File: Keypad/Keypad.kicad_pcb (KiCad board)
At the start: 2 copper layers, 50 x 35 mm, 3 parts, among them J1 locked

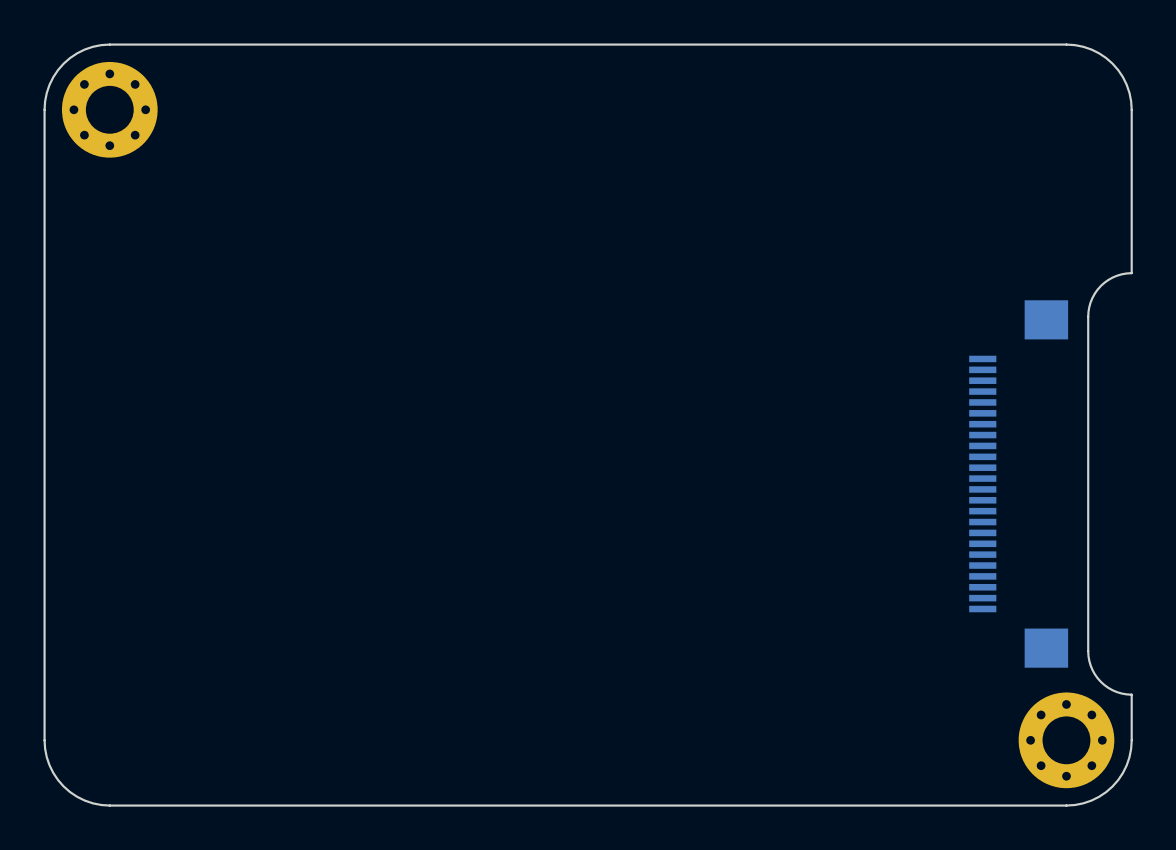
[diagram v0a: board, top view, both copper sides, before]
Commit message: Roughly places components in the keypad PCB
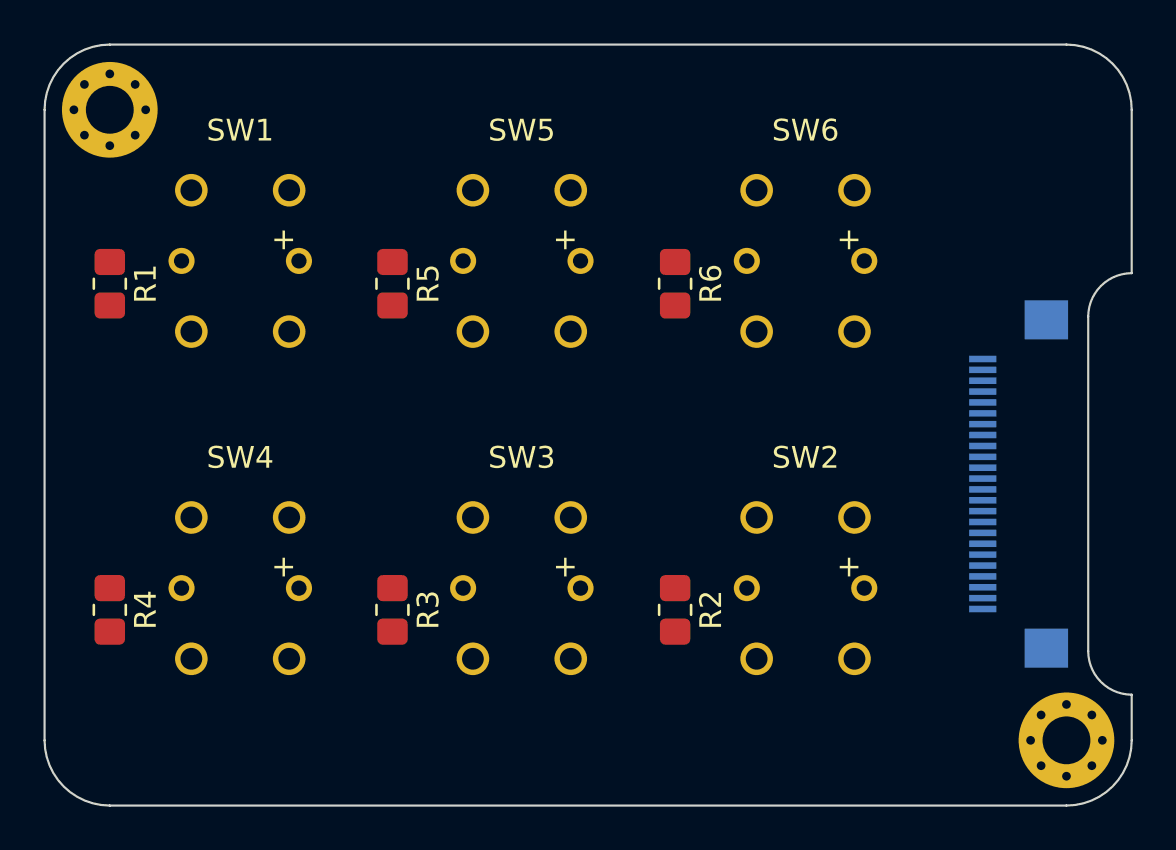
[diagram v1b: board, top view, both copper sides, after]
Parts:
- added R1: 100Ω, Resistor_SMD:R_0805_2012Metric_Pad1.20x1.40mm_HandSolder, F.Cu at (123.0, 91.0)
- added R2: 100Ω, Resistor_SMD:R_0805_2012Metric_Pad1.20x1.40mm_HandSolder, F.Cu at (149.0, 106.0)
- added R3: 100Ω, Resistor_SMD:R_0805_2012Metric_Pad1.20x1.40mm_HandSolder, F.Cu at (136.0, 106.0)
- added R4: 100Ω, Resistor_SMD:R_0805_2012Metric_Pad1.20x1.40mm_HandSolder, F.Cu at (123.0, 106.0)
- added R5: 100Ω, Resistor_SMD:R_0805_2012Metric_Pad1.20x1.40mm_HandSolder, F.Cu at (136.0, 91.0)
- added R6: 100Ω, Resistor_SMD:R_0805_2012Metric_Pad1.20x1.40mm_HandSolder, F.Cu at (149.0, 91.0)
- added SW1: TL1240GQ1JCLR, GameOver:TL1240GQ1JCLR, F.Cu at (129.0, 90.0)
- added SW2: TL1240GQ1JCLR, GameOver:TL1240GQ1JCLR, F.Cu at (155.0, 105.0)
- added SW3: TL1240GQ1JCLR, GameOver:TL1240GQ1JCLR, F.Cu at (141.9, 105.0)
- added SW4: TL1240GQ1JCLR, GameOver:TL1240GQ1JCLR, F.Cu at (129.0, 105.0)
- added SW5: TL1240GQ1JCLR, GameOver:TL1240GQ1JCLR, F.Cu at (141.9, 90.0)
- added SW6: TL1240GQ1JCLR, GameOver:TL1240GQ1JCLR, F.Cu at (155.0, 90.0)
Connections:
- J1 pad 17: unconnected-(J1-IO33) -> SW_6
- J1 pad 18: unconnected-(J1-IO25) -> LED_6
- J1 pad 19: unconnected-(J1-IO26) -> SW_4
- J1 pad 20: unconnected-(J1-IO27) -> LED_4
- J1 pad 21: unconnected-(J1-IO2) -> SW_2
- J1 pad 22: unconnected-(J1-IO15) -> LED_2
- J1 pad 3: unconnected-(J1-IO23) -> SW_1
- J1 pad 4: unconnected-(J1-IO22) -> LED_1
- J1 pad 5: unconnected-(J1-IO21) -> SW_3
- J1 pad 6: unconnected-(J1-IO19) -> LED_3
- J1 pad 7: unconnected-(J1-IO5) -> SW_5
- J1 pad 8: unconnected-(J1-IO18) -> LED_5

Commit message: Reorganizes components for better placement in keypad
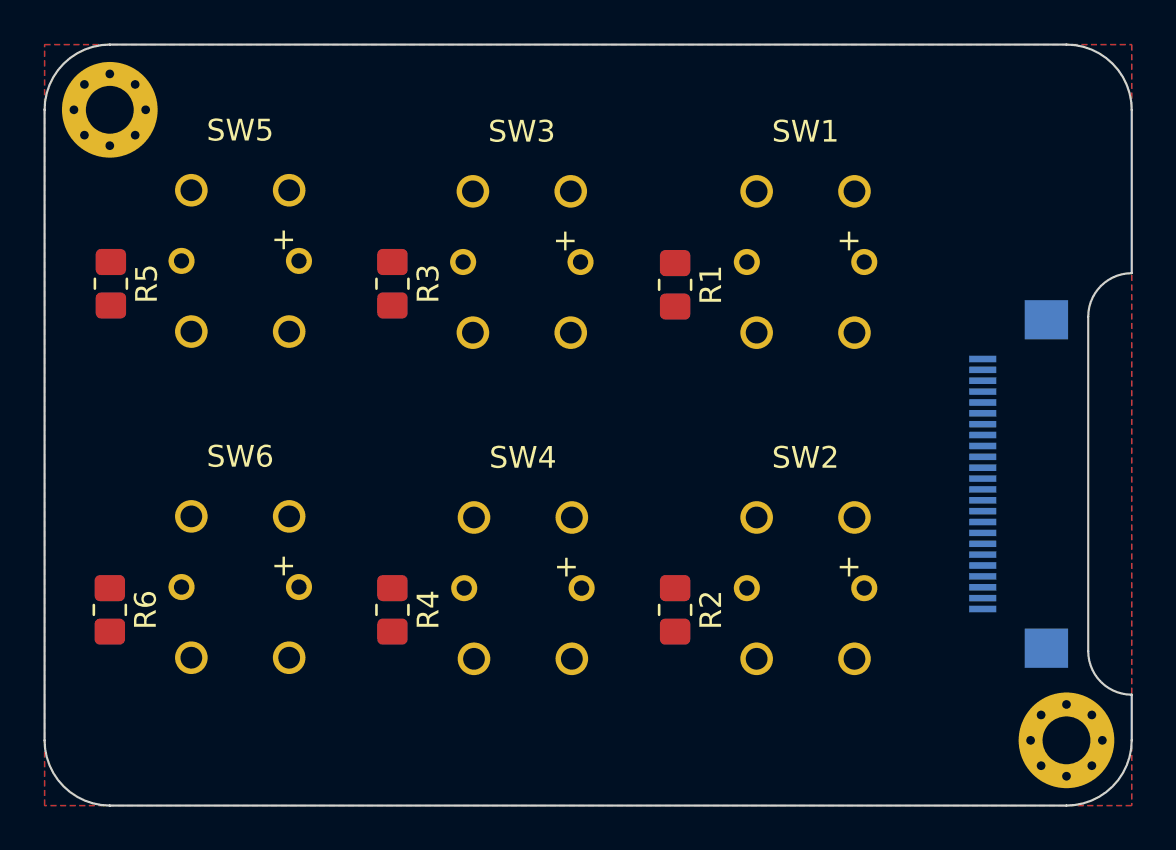
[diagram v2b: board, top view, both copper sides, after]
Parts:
- moved R6 30.0 mm to (123.0, 106.0)
- moved SW6 30.0 mm to (129.0, 105.0)
- moved R1 26.0 mm to (149.0, 91.0)
- moved SW1 26.0 mm to (155.0, 90.0)
- moved R3 15.0 mm to (136.0, 91.0)
- moved SW3 15.0 mm to (141.9, 90.0)
- moved R4 13.0 mm to (136.0, 106.0)
- moved SW4 13.0 mm to (142.0, 105.0)
- moved R5 13.0 mm to (123.0, 91.0)
- moved SW5 12.9 mm to (129.0, 90.0)
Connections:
- SW1 pad 3: SW_1 -> unconnected-(SW1-Pad3)
- SW2 pad 4: SW_2 -> unconnected-(SW2-Pad4)
- SW3 pad 3: SW_3 -> unconnected-(SW3-Pad3)
- SW4 pad 4: SW_4 -> unconnected-(SW4-Pad4)
- SW5 pad 3: SW_5 -> unconnected-(SW5-Pad3)
- SW6 pad 4: SW_6 -> unconnected-(SW6-Pad4)
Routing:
- added copper zone on B.Cu, net +3V3
- added copper zone on F.Cu, net GND
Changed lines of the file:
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@@
   (net 25 "Net-(SW5--)")
   (net 26 "Net-(SW6--)")
+  (net 27 "unconnected-(SW1-Pad3)")
+  (net 28 "unconnected-(SW2-Pad4)")
+  (net 29 "unconnected-(SW3-Pad3)")
+  (net 30 "unconnected-(SW4-Pad4)")
+  (net 31 "unconnected-(SW5-Pad3)")
+  (net 32 "unconnected-(SW6-Pad4)")
   (footprint "Resistor_SMD:R_0805_2012Metric_Pad1.20x1.40mm_HandSolder" (layer "F.Cu")
-    (at 136 91 -90)
+    (at 123.05 91 -90)
     (descr "Resistor SMD 0805 (2012 Metric), square (rectangular) end terminal, IPC_7351 nominal with elongated pad for handsoldering. (Body size source: IPC-SM-782 page 72, https://www.pcb-3d.com/wordpress/wp-content/uploads/ipc-sm-782a_amendment_1_and_2.pdf), generated with kicad-footprint-generator")
     (tags "resistor handsolder")
@@
       (net 19 "SW_2") (pinfunction "3") (pintype "passive"))
     (pad "4" thru_hole circle (at -2.25 3.25) (size 1.5 1.5) (drill 1) (layers *.Cu *.Mask)
-      (net 19 "SW_2") (pinfunction "4") (pintype "passive"))
+      (net 28 "unconnected-(SW2-Pad4)") (pinfunction "4") (pintype "passive+no_connect"))
     (pad "5" thru_hole circle (at 2.7 0) (size 1.2 1.2) (drill 0.7) (layers *.Cu *.Mask)
       (net 20 "LED_2") (pinfunction "+") (pintype "passive"))
@@
   )
   (footprint "GameOver:TL1240GQ1JCLR" (layer "F.Cu")
-    (at 141.95 105)
+    (at 141.95 90)
     (property "Sheetfile" "Keypad.kicad_sch")
     (property "Sheetname" "")
@@
       (net 2 "+3V3") (pinfunction "2") (pintype "passive"))
     (pad "3" thru_hole circle (at -2.25 -3.25) (size 1.5 1.5) (drill 1) (layers *.Cu *.Mask)
-      (net 5 "SW_3") (pinfunction "3") (pintype "passive"))
+      (net 29 "unconnected-(SW3-Pad3)") (pinfunction "3") (pintype "passive+no_connect"))
     (pad "4" thru_hole circle (at -2.25 3.25) (size 1.5 1.5) (drill 1) (layers *.Cu *.Mask)
       (net 5 "SW_3") (pinfunction "4") (pintype "passive"))
@@
   )
   (footprint "Resistor_SMD:R_0805_2012Metric_Pad1.20x1.40mm_HandSolder" (layer "F.Cu")
-    (at 123 106 -90)
+    (at 136 106 -90)
     (descr "Resistor SMD 0805 (2012 Metric), square (rectangular) end terminal, IPC_7351 nominal with elongated pad for handsoldering. (Body size source: IPC-SM-782 page 72, https://www.pcb-3d.com/wordpress/wp-content/uploads/ipc-sm-782a_amendment_1_and_2.pdf), generated with kicad-footprint-generator")
     (tags "resistor handsolder")
@@
   )
   (footprint "GameOver:TL1240GQ1JCLR" (layer "F.Cu")
-    (at 129 105)
+    (at 142 105)
     (property "Sheetfile" "Keypad.kicad_sch")
     (property "Sheetname" "")
@@
       (net 14 "SW_4") (pinfunction "3") (pintype "passive"))
     (pad "4" thru_hole circle (at -2.25 3.25) (size 1.5 1.5) (drill 1) (layers *.Cu *.Mask)
-      (net 14 "SW_4") (pinfunction "4") (pintype "passive"))
+      (net 30 "unconnected-(SW4-Pad4)") (pinfunction "4") (pintype "passive+no_connect"))
     (pad "5" thru_hole circle (at 2.7 0) (size 1.2 1.2) (drill 0.7) (layers *.Cu *.Mask)
       (net 18 "LED_4") (pinfunction "+") (pintype "passive"))
@@
   )
   (footprint "Resistor_SMD:R_0805_2012Metric_Pad1.20x1.40mm_HandSolder" (layer "F.Cu")
-    (at 136 106 -90)
+    (at 136 91 -90)
     (descr "Resistor SMD 0805 (2012 Metric), square (rectangular) end terminal, IPC_7351 nominal with elongated pad for handsoldering. (Body size source: IPC-SM-782 page 72, https://www.pcb-3d.com/wordpress/wp-content/uploads/ipc-sm-782a_amendment_1_and_2.pdf), generated with kicad-footprint-generator")
     (tags "resistor handsolder")
@@
   )
   (footprint "Resistor_SMD:R_0805_2012Metric_Pad1.20x1.40mm_HandSolder" (layer "F.Cu")
-    (at 123 91 -90)
+    (at 149 91.05 -90)
     (descr "Resistor SMD 0805 (2012 Metric), square (rectangular) end terminal, IPC_7351 nominal with elongated pad for handsoldering. (Body size source: IPC-SM-782 page 72, https://www.pcb-3d.com/wordpress/wp-content/uploads/ipc-sm-782a_amendment_1_and_2.pdf), generated with kicad-footprint-generator")
     (tags "resistor handsolder")
@@
   )
   (footprint "Resistor_SMD:R_0805_2012Metric_Pad1.20x1.40mm_HandSolder" (layer "F.Cu")
-    (at 149 91 -90)
+    (at 123 106 -90)
     (descr "Resistor SMD 0805 (2012 Metric), square (rectangular) end terminal, IPC_7351 nominal with elongated pad for handsoldering. (Body size source: IPC-SM-782 page 72, https://www.pcb-3d.com/wordpress/wp-content/uploads/ipc-sm-782a_amendment_1_and_2.pdf), generated with kicad-footprint-generator")
     (tags "resistor handsolder")
@@
   )
   (footprint "GameOver:TL1240GQ1JCLR" (layer "F.Cu")
-    (at 155 89.95)
+    (at 129 104.95)
     (property "Sheetfile" "Keypad.kicad_sch")
     (property "Sheetname" "")
@@
         (effects (font (size 1 1) (thickness 0.15)))
     )
-    (fp_text value "TL1240GQ1JCLR" (at 0 12 unlocked) (layer "F.Fab")
+    (fp_text value "TL1240GQ1JCLR" (at 0 6.05 unlocked) (layer "F.Fab")
         (effects (font (size 1 1) (thickness 0.15)))
     )
@@
         (effects (font (size 1 1) (thickness 0.15)))
     )
-    (fp_text user "${REFERENCE}" (at 0 14 unlocked) (layer "F.Fab")
+    (fp_text user "${REFERENCE}" (at 0 8.05 unlocked) (layer "F.Fab")
         (effects (font (size 1 1) (thickness 0.15)))
     )
@@
       (net 9 "SW_6") (pinfunction "3") (pintype "passive"))
     (pad "4" thru_hole circle (at -2.25 3.25) (size 1.5 1.5) (drill 1) (layers *.Cu *.Mask)
-      (net 9 "SW_6") (pinfunction "4") (pintype "passive"))
+      (net 32 "unconnected-(SW6-Pad4)") (pinfunction "4") (pintype "passive+no_connect"))
     (pad "5" thru_hole circle (at 2.7 0) (size 1.2 1.2) (drill 0.7) (layers *.Cu *.Mask)
       (net 13 "LED_6") (pinfunction "+") (pintype "passive"))
@@
   )
   (footprint "GameOver:TL1240GQ1JCLR" (layer "F.Cu")
-    (at 129 89.95)
+    (at 155 90)
     (property "Sheetfile" "Keypad.kicad_sch")
     (property "Sheetname" "")
@@
         (effects (font (size 1 1) (thickness 0.15)))
     )
-    (fp_text value "TL1240GQ1JCLR" (at 0 12 unlocked) (layer "F.Fab")
+    (fp_text value "TL1240GQ1JCLR" (at 0 6 unlocked) (layer "F.Fab")
         (effects (font (size 1 1) (thickness 0.15)))
     )
@@
         (effects (font (size 1 1) (thickness 0.15)))
     )
-    (fp_text user "${REFERENCE}" (at 0 14 unlocked) (layer "F.Fab")
+    (fp_text user "${REFERENCE}" (at 0 8 unlocked) (layer "F.Fab")
         (effects (font (size 1 1) (thickness 0.15)))
     )
@@
       (net 2 "+3V3") (pinfunction "2") (pintype "passive"))
     (pad "3" thru_hole circle (at -2.25 -3.25) (size 1.5 1.5) (drill 1) (layers *.Cu *.Mask)
-      (net 3 "SW_1") (pinfunction "3") (pintype "passive"))
+      (net 27 "unconnected-(SW1-Pad3)") (pinfunction "3") (pintype "passive+no_connect"))
     (pad "4" thru_hole circle (at -2.25 3.25) (size 1.5 1.5) (drill 1) (layers *.Cu *.Mask)
       (net 3 "SW_1") (pinfunction "4") (pintype "passive"))
@@
   )
   (footprint "GameOver:TL1240GQ1JCLR" (layer "F.Cu")
-    (at 141.95 89.95)
+    (at 129 89.95)
     (property "Sheetfile" "Keypad.kicad_sch")
     (property "Sheetname" "")
@@
         (effects (font (size 1 1) (thickness 0.15)))
     )
-    (fp_text value "TL1240GQ1JCLR" (at 0 12 unlocked) (layer "F.Fab")
+    (fp_text value "TL1240GQ1JCLR" (at 0 6.05 unlocked) (layer "F.Fab")
         (effects (font (size 1 1) (thickness 0.15)))
     )
@@
         (effects (font (size 1 1) (thickness 0.15)))
     )
-    (fp_text user "${REFERENCE}" (at 0 14 unlocked) (layer "F.Fab")
+    (fp_text user "${REFERENCE}" (at 0 8.05 unlocked) (layer "F.Fab")
         (effects (font (size 1 1) (thickness 0.15)))
     )
@@
       (net 2 "+3V3") (pinfunction "2") (pintype "passive"))
     (pad "3" thru_hole circle (at -2.25 -3.25) (size 1.5 1.5) (drill 1) (layers *.Cu *.Mask)
-      (net 7 "SW_5") (pinfunction "3") (pintype "passive"))
+      (net 31 "unconnected-(SW5-Pad3)") (pinfunction "3") (pintype "passive+no_connect"))
     (pad "4" thru_hole circle (at -2.25 3.25) (size 1.5 1.5) (drill 1) (layers *.Cu *.Mask)
       (net 7 "SW_5") (pinfunction "4") (pintype "passive"))
@@
   (gr_arc locked (start 167 80) (mid 169.12132 80.87868) (end 170 83)
     (stroke (width 0.1) (type default)) (layer "Edge.Cuts"))
+  (zone (net 1) (net_name "GND") (layer "F.Cu") (hatch edge 0.508)
+    (connect_pads (clearance 0.508))
+    (min_thickness 0.254) (filled_areas_thickness no)
+    (fill yes (thermal_gap 0.508) (thermal_bridge_width 0.508) (island_removal_mode 2) (island_area_min 10))
+    (polygon
+      (pts
+        (xy 170 115)
+        (xy 120 115)
+        (xy 120 80)
+        (xy 170 80)
+      )
+    )
+  )
+  (zone (net 2) (net_name "+3V3") (layer "B.Cu") (hatch edge 0.508)
+    (connect_pads (clearance 0.508))
+    (min_thickness 0.254) (filled_areas_thickness no)
+    (fill yes (thermal_gap 0.508) (thermal_bridge_width 0.508) (island_removal_mode 2) (island_area_min 10))
+    (polygon
+      (pts
+        (xy 170 115)
+        (xy 120 115)
+        (xy 120 80)
+        (xy 170 80)
+      )
+    )
+  )
 )

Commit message: Swaps switch and led pins for top row
This will make it easier to route the top buttons.
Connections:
- J1 pad 3: SW_1 -> LED_1
- J1 pad 4: LED_1 -> unconnected-(J1-IO22)
- J1 pad 5: SW_3 -> LED_3
- J1 pad 6: LED_3 -> SW_3
- J1 pad 7: SW_5 -> LED_5
- J1 pad 8: LED_5 -> SW_5
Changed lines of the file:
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@@
   (net 31 "unconnected-(SW5-Pad3)")
   (net 32 "unconnected-(SW6-Pad4)")
+  (net 33 "unconnected-(J1-IO22)")
   (footprint "Resistor_SMD:R_0805_2012Metric_Pad1.20x1.40mm_HandSolder" (layer "F.Cu")
     (at 123.05 91 -90)
@@
       (net 2 "+3V3") (pinfunction "3v3") (pintype "power_in"))
     (pad "3" smd rect locked (at -4.75 1.85 270) (size 0.3 1.25) (layers "B.Cu" "B.Paste" "B.Mask")
-      (net 3 "SW_1") (pinfunction "IO23") (pintype "bidirectional"))
+      (net 4 "LED_1") (pinfunction "IO23") (pintype "bidirectional"))
     (pad "4" smd rect locked (at -4.25 1.85 270) (size 0.3 1.25) (layers "B.Cu" "B.Paste" "B.Mask")
-      (net 4 "LED_1") (pinfunction "IO22") (pintype "bidirectional"))
+      (net 33 "unconnected-(J1-IO22)") (pinfunction "IO22") (pintype "bidirectional"))
     (pad "5" smd rect locked (at -3.75 1.85 270) (size 0.3 1.25) (layers "B.Cu" "B.Paste" "B.Mask")
-      (net 5 "SW_3") (pinfunction "IO21") (pintype "bidirectional"))
+      (net 6 "LED_3") (pinfunction "IO21") (pintype "bidirectional"))
     (pad "6" smd rect locked (at -3.25 1.85 270) (size 0.3 1.25) (layers "B.Cu" "B.Paste" "B.Mask")
-      (net 6 "LED_3") (pinfunction "IO19") (pintype "bidirectional"))
+      (net 5 "SW_3") (pinfunction "IO19") (pintype "bidirectional"))
     (pad "7" smd rect locked (at -2.75 1.85 270) (size 0.3 1.25) (layers "B.Cu" "B.Paste" "B.Mask")
-      (net 7 "SW_5") (pinfunction "IO5") (pintype "bidirectional"))
+      (net 8 "LED_5") (pinfunction "IO5") (pintype "bidirectional"))
     (pad "8" smd rect locked (at -2.25 1.85 270) (size 0.3 1.25) (layers "B.Cu" "B.Paste" "B.Mask")
-      (net 8 "LED_5") (pinfunction "IO18") (pintype "bidirectional"))
+      (net 7 "SW_5") (pinfunction "IO18") (pintype "bidirectional"))
     (pad "9" smd rect locked (at -1.75 1.85 270) (size 0.3 1.25) (layers "B.Cu" "B.Paste" "B.Mask")
       (net 10 "unconnected-(J1-IO17)") (pinfunction "IO17") (pintype "bidirectional+no_connect"))
